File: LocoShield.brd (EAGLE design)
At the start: 50 x 50 mm, 28 parts, among them J2 RJ12/6, J3 RJ12/6, Q1 2N3904, U1 LM393M, U2 LM317LCDR

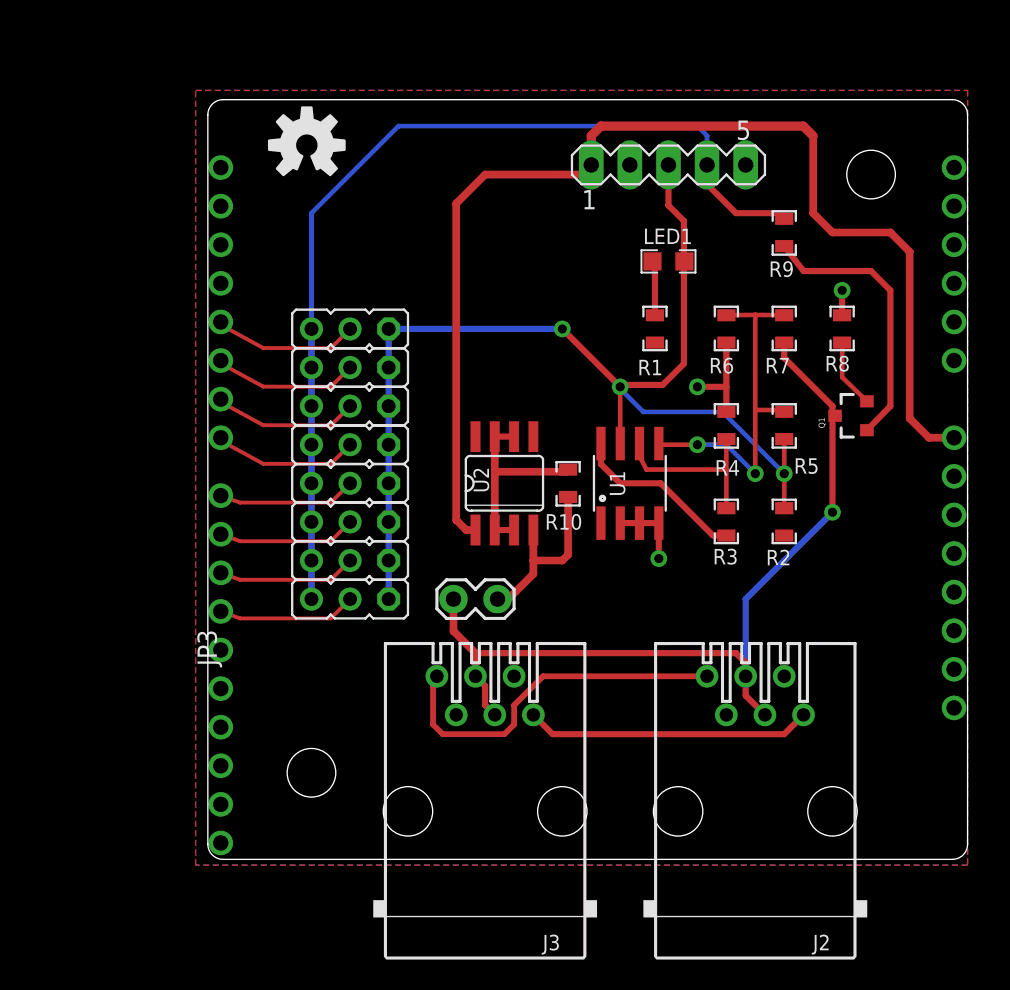
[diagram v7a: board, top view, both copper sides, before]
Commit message: normalized values
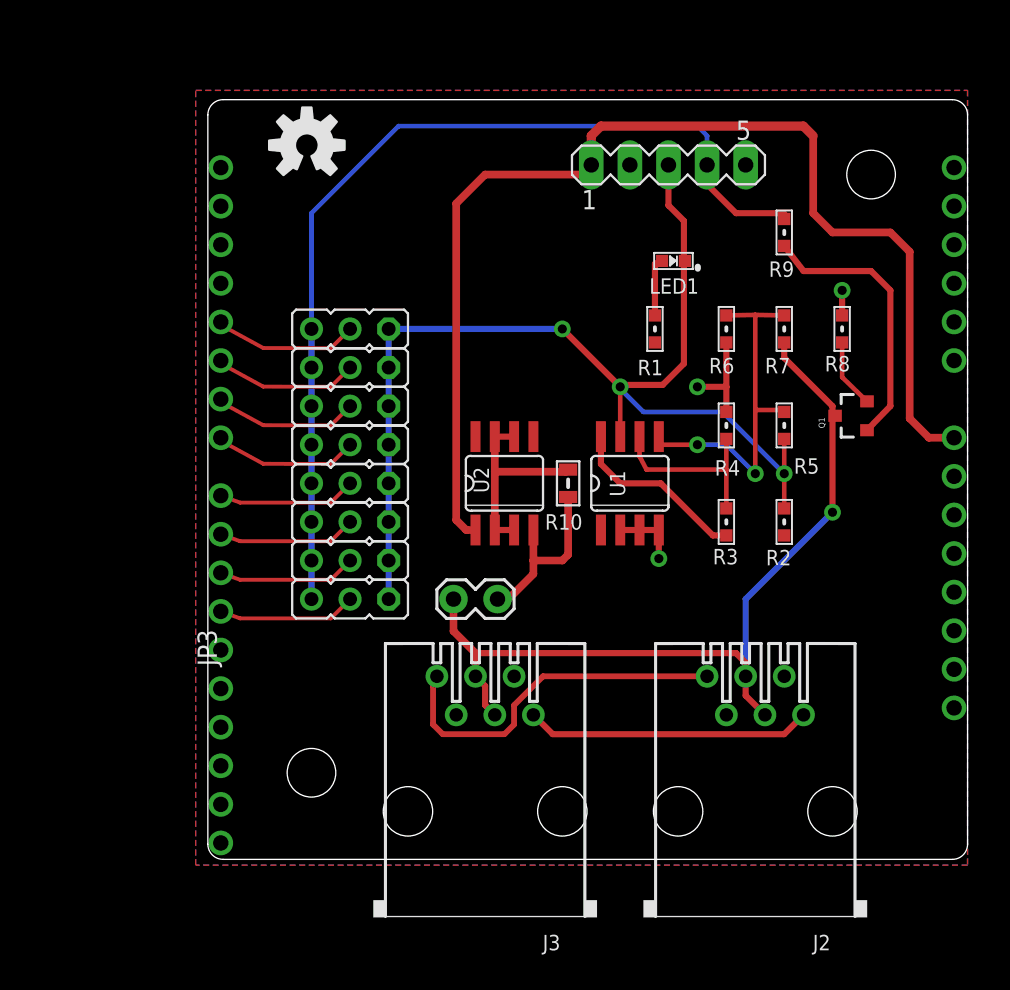
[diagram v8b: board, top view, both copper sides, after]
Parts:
- J2, J3: device con-amp:520250-3 -> SPCoast:RJ25-PANEL
- JP3: value LN-TERM -> 0.100
- LED1: value Blue -> B; device SPCoast:0805-LED -> SPCoast:0603-LED
- R1, R2, R3, R4, R5, R6, R7, R8, R9: device SPCoast:0805-RES -> SPCoast:0603-RES
- SHIELD: value ARDUINO_SHIELDNO_SILK -> ARDUINO_SHIELD
- U$1: value OSHW-LOGOM -> OSHW
- U1: device MCP:SO08@1 -> MCP:SO08
- moved LED1 0.33 mm to (30.6, 39.4), turned to 180 degrees
